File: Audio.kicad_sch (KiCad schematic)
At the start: 27 parts, among them J7 0532610271, U11 TAS2505IRGER

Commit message: Layout draft complete
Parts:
- removed LS1: CMS-151135-078S, jka_library:CMS-151135-078S, symbol jka_library:CMS-151135-078S
- removed R41: 0k, Resistor_SMD:R_0603_1608Metric, symbol Device:R_US
- removed R44, R45, R50, R51: 0R, Resistor_SMD:R_0603_1608Metric, symbol Device:R_US
- added C77: 1 uF, Capacitor_SMD:C_0603_1608Metric, symbol Device:C
- added D11: LED, Diode_SMD:D_0603_1608Metric, symbol Device:LED
- added J19, J9: Conn_01x02_Pin, Connector_PinHeader_2.54mm:PinHeader_1x02_P2.54mm_Vertical, symbol Connector:Conn_01x02_Pin
- added J20: Conn_01x04_Pin, Connector_PinHeader_2.54mm:PinHeader_1x04_P2.54mm_Vertical, symbol Connector:Conn_01x04_Pin
- added R23: 1k, Resistor_SMD:R_0603_1608Metric, symbol Device:R_US
- added SW3: TPS22919DCKR, jka_library:SOT65P210X110-6N, symbol jka_library:TPS22919DCKR
- C54, C55: value 0.1 uF -> 1 uF
- J7: now fitted
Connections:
- net +3V3: now also C77.1, SW3.1 (IN)
- net AINL: now also C54.1
- net AINL_IN: now also J9.2 (Pin_2)
- net AINR: now also C55.1
- net AINR_IN: now also J9.1 (Pin_1)
- net GND: now also C77.2, J19.1 (Pin_1), R23.2, SW3.2 (GND)
- net HPOUT_P: now also J19.2 (Pin_2)
- net IOVDD: now also SW3.5 (QOD), SW3.6 (OUT)
- net SPK_OUT_M: now also C57.2, C59.2, J7.1, L5.2
- net SPK_OUT_P: now also J7.2
- net GPIO/DOUT: no longer names the net of U11.18 (GPIO_DOUT)
- net GPIO/DOUT: now also D11.2 (A)
- net I2S_BCLK renamed SAI_SCK_B/SWO
- net SAI_SCK_B/SWO: now also J20.2 (Pin_2)
- net I2S_DIN renamed SAI_SD_B
- net SAI_SD_B: now also J20.1 (Pin_1)
- net I2S_WCLK renamed SAI_FS_B
- net SAI_FS_B: now also J20.4 (Pin_4)
- net INTx renamed AUDIO_GPIO
- net MCLK renamed SAI_MCLK_B
- net SAI_MCLK_B: now also J20.3 (Pin_3)
- net ~{RST} renamed ~{AUDIO_RST}
- new net: D11.1 (K), R23.1
- new net AUDIO_IOVDD_EN: SW3.3 (ON)
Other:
- note added: "No pulldown needed, smart one included"
- title: (none) -> Jakka1
- moved on the sheet: C53, C54, C55, C56, C57, C58, C59, L4, L5, R40, R43, U11

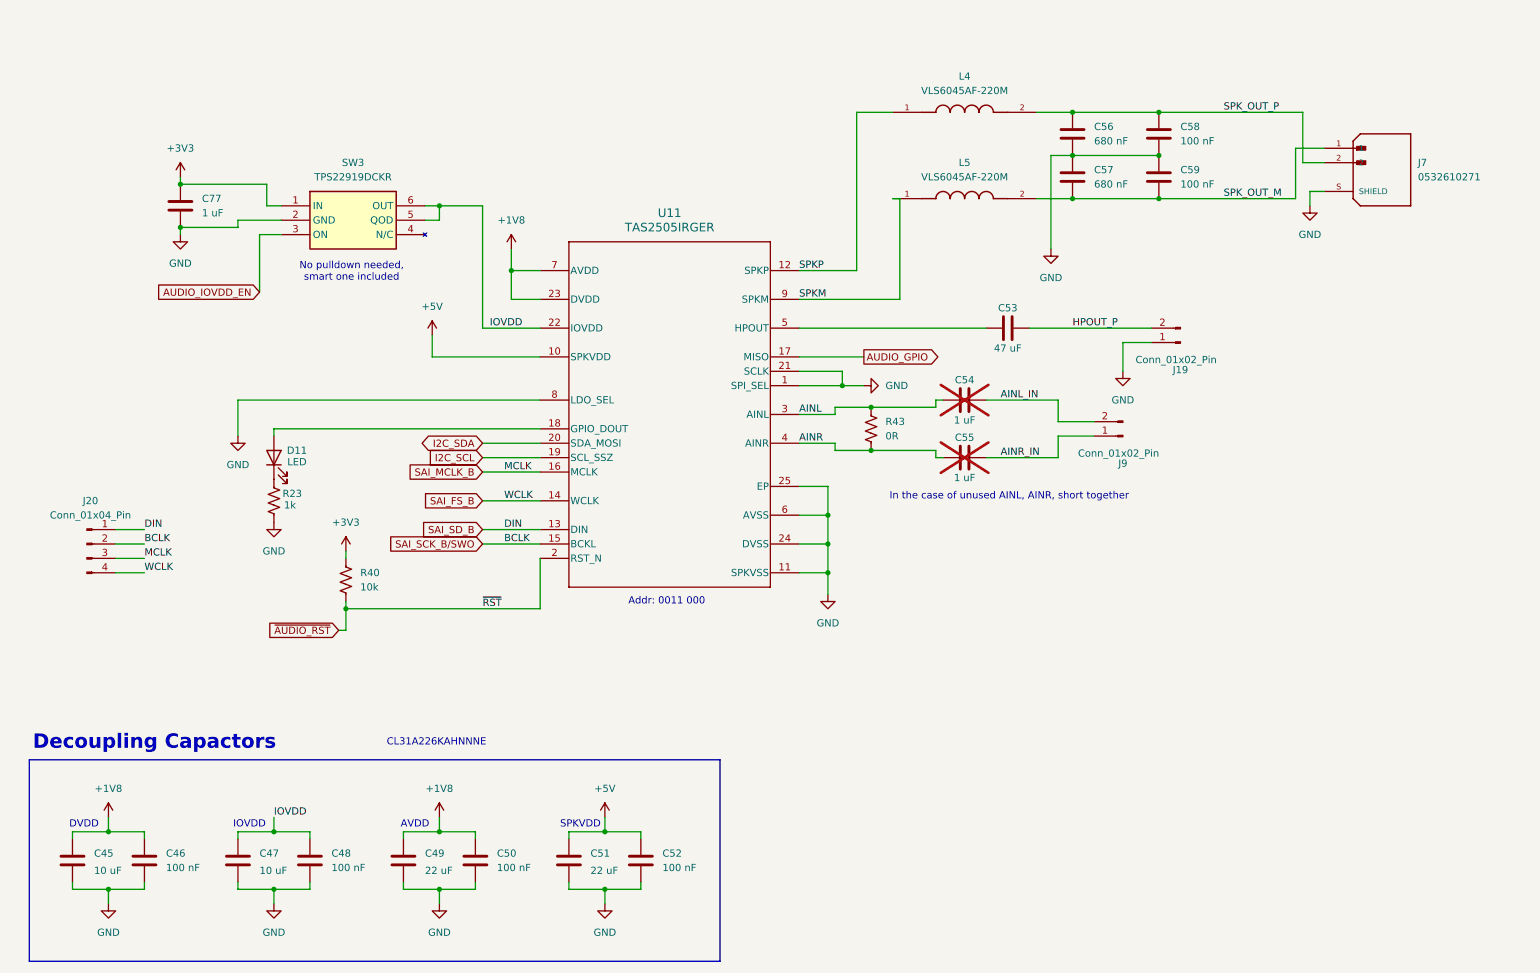
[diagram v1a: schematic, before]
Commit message: First draft of design output, schematic, and layout complete
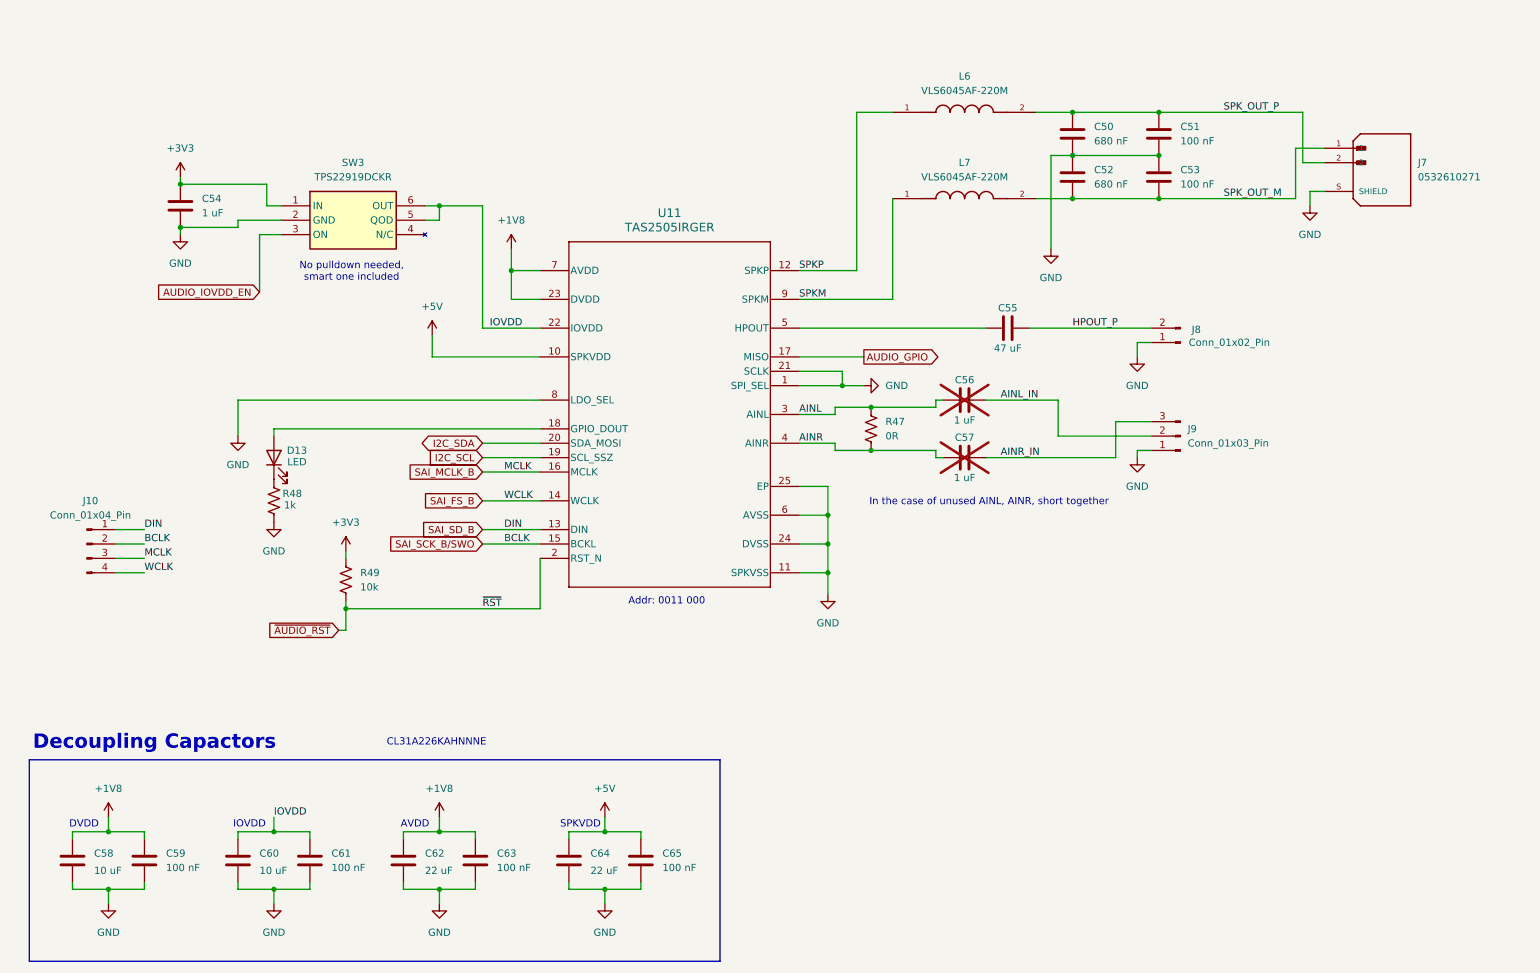
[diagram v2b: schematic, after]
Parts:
- removed J9: Conn_01x02_Pin, Connector_PinHeader_2.54mm:PinHeader_1x02_P2.54mm_Vertical, symbol Connector:Conn_01x02_Pin
- added J9: Conn_01x03_Pin, Connector_PinHeader_2.54mm:PinHeader_1x03_P2.54mm_Vertical, symbol Connector:Conn_01x03_Pin
- renumbered C56 to C50, C58 to C51, C57 to C52, C59 to C53, C77 to C54, C53 to C55, C54 to C56, C55 to C57, C45 to C58, C46 to C59, C47 to C60, C48 to C61, C49 to C62, C50 to C63, C51 to C64, C52 to C65, D11 to D13, J20 to J10, J19 to J8, L4 to L6, L5 to L7, R43 to R47, R23 to R48, R40 to R49
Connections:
- net AINL_IN: now also J9.2 (Pin_2)
- net AINR_IN: now also J9.3 (Pin_3)
- net GND: now also J9.1 (Pin_1)
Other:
- company: (none) -> Jacob Kapala
